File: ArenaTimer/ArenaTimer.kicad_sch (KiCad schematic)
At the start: 2 parts, among them U1 LM2596S-5

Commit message: finish up routing
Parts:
- removed A1: Adafruit_Feather_HUZZAH32_ESP32, Module:Adafruit_Feather, symbol MCU_Module:Adafruit_Feather_HUZZAH32_ESP32
- removed U1: LM2596S-5, Package_TO_SOT_SMD:TO-263-5_TabPin3, symbol Regulator_Switching:LM2596S-5
- added J1: POWER IN, TerminalBlock:TerminalBlock_Altech_AK300-2_P5.00mm, symbol Connector:Screw_Terminal_01x02
- added J2, J3: Conn_01x02_Pin, Connector_PinHeader_2.54mm:PinHeader_1x02_P2.54mm_Vertical, symbol Connector:Conn_01x02_Pin
- added J4, J6: GND, Connector_PinHeader_2.54mm:PinHeader_1x04_P2.54mm_Vertical, symbol Connector:Conn_01x04_Pin
- added J5, J7: 5V, Connector_PinHeader_2.54mm:PinHeader_1x04_P2.54mm_Vertical, symbol Connector:Conn_01x04_Pin
- added JP1: Jumper_2_Open, Jumper:SolderJumper-2_P1.3mm_Open_RoundedPad1.0x1.5mm, symbol Jumper:Jumper_2_Open
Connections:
- net TimerBorder/DIN: now also J2.2 (Pin_2), JP1.1 (A)
- net TimerBorder/DOUT: now also J3.2 (Pin_2)
- net TimerColon/DOUT: now also J3.1 (Pin_1), JP1.2 (B)
- new net +5V: J1.2 (Pin_2), J5.1 (Pin_1), J5.2 (Pin_2), J5.3 (Pin_3), J5.4 (Pin_4), J7.1 (Pin_1), J7.2 (Pin_2), J7.3 (Pin_3), J7.4 (Pin_4)
- new net GND: J1.1 (Pin_1), J4.1 (Pin_1), J4.2 (Pin_2), J4.3 (Pin_3), J4.4 (Pin_4), J6.1 (Pin_1), J6.2 (Pin_2), J6.3 (Pin_3), J6.4 (Pin_4)
- new net TimerDigit6/DIN: J2.1 (Pin_1)
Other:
- removed sheet TimerBorder1
- removed sheet TimerColon1
- removed sheet TimerDigit1
- removed sheet TimerDigit2
- removed sheet TimerDigit3
- removed sheet TimerDigit4
- removed sheet TimerDigit5
- added sheet TimerDigit6 (TimerDigit.kicad_sch)
- note added: "2nd copy of board is rotated 180 and makes up the other half of the display"
- note added: "5V Power Input"
- note added: "IO IN"
- note added: "IO OUT"
- note added: "Power connections between boards"
- note removed: "Back Side"
- note removed: "Front Side"
- note removed: "MCU ...."
- note removed: "Power 5V, 3A"

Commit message: add 3d models
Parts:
- removed J1: POWER IN, TerminalBlock:TerminalBlock_Altech_AK300-2_P5.00mm, symbol Connector:Screw_Terminal_01x02
- removed J2: Conn_01x02_Pin, Connector_PinHeader_2.54mm:PinHeader_1x02_P2.54mm_Vertical, symbol Connector:Conn_01x02_Pin
- removed J6: GND, Connector_PinHeader_2.54mm:PinHeader_1x04_P2.54mm_Vertical, symbol Connector:Conn_01x04_Pin
- removed J7: 5V, Connector_PinHeader_2.54mm:PinHeader_1x04_P2.54mm_Vertical, symbol Connector:Conn_01x04_Pin
- added D40: 1N1007, SMA, Diode_SMD:D_SMA, symbol Device:D
- added H1, H2, H3, H4, H5, H6, H7, H8, H9: MountingHole, MountingHole:MountingHole_3.2mm_M3, symbol Mechanical:MountingHole
- added J1: Blue ready-up, Connector_JST:JST_EH_S2B-EH_1x02_P2.50mm_Horizontal, symbol Connector:Conn_01x02_Socket
- added J10: Red ready-up, Connector_JST:JST_EH_S2B-EH_1x02_P2.50mm_Horizontal, symbol Connector:Conn_01x02_Socket
- added J11: Bell Power, TerminalBlock:TerminalBlock_bornier-2_P5.08mm, symbol Connector:Screw_Terminal_01x02
- added J12, J13: Screw_Terminal_01x03, TerminalBlock:TerminalBlock_bornier-3_P5.08mm, symbol Connector:Screw_Terminal_01x03
- added J15, J16: Conn_01x15_Socket, Connector_PinSocket_2.54mm:PinSocket_1x15_P2.54mm_Vertical, symbol Connector:Conn_01x15_Socket
- added J2: Conn_01x02_Socket, Connector_PinSocket_2.54mm:PinSocket_1x02_P2.54mm_Horizontal, symbol Connector:Conn_01x02_Socket
- added J6: GND, Connector_PinSocket_2.54mm:PinSocket_1x04_P2.54mm_Horizontal, symbol Connector:Conn_01x04_Socket
- added J7: 5V, Connector_PinSocket_2.54mm:PinSocket_1x04_P2.54mm_Horizontal, symbol Connector:Conn_01x04_Socket
- added J8: Barrel_Jack, Connector_BarrelJack:BarrelJack_Horizontal, symbol Connector:Barrel_Jack
- added J9: Conn_01x06_Pin, Connector_JST:JST_EH_S6B-EH_1x06_P2.50mm_Horizontal, symbol Connector:Conn_01x06_Pin
- added K1: G5V-2_Split, Relay_THT:Relay_DPDT_Omron_G5V-2, symbol Relay:G5V-2_Split
- added Q1: BSS214NW, Package_TO_SOT_SMD:SOT-323_SC-70, symbol Transistor_FET:BSS214NW
- added R2: 100K, Resistor_SMD:R_0402_1005Metric, symbol Device:R_US
- J3: footprint Connector_PinHeader_2.54mm:PinHeader_1x02_P2.54mm_Vertical -> Connector_PinHeader_2.54mm:PinHeader_1x02_P2.54mm_Horizontal
- J4, J5: footprint Connector_PinHeader_2.54mm:PinHeader_1x04_P2.54mm_Vertical -> Connector_PinHeader_2.54mm:PinHeader_1x04_P2.54mm_Horizontal
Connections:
- net +5V: now also JP1.2 (B), D40.1 (K), J15.15 (Pin_15), J7.1 (Pin_1), J7.2 (Pin_2), J7.3 (Pin_3), J7.4 (Pin_4), J8.1, K1.1
- net GND: now also J1.2 (Pin_2), J10.2 (Pin_2), J11.2 (Pin_2), J12.3 (Pin_3), J13.3 (Pin_3), J15.14 (Pin_14), J16.14 (Pin_14), J6.1 (Pin_1), J6.2 (Pin_2), J6.3 (Pin_3), J6.4 (Pin_4), J8.2, J9.6 (Pin_6), Q1.2 (S), R2.2
- net TimerColon/DOUT: no longer JP1.2 (B)
- net TimerBorder/DIN: no longer names the net of JP1.1 (A)
- net TimerBorder/DIN: now also J11.1 (Pin_1), K1.13, K1.4
- new net: J12.1 (Pin_1), K1.6
- new net: J12.2 (Pin_2), K1.8
- new net: J13.1 (Pin_1), K1.11
- new net: J13.2 (Pin_2), K1.9
- new net: D40.2 (A), K1.16, Q1.3 (D)
- new net +3.3V: J16.15 (Pin_15)
- new net BORDER_LEDS: J16.9 (Pin_9), J2.1 (Pin_1)
- new net DIGIT_LEDS: J16.8 (Pin_8), J2.2 (Pin_2)
- new net RELAY_EN: J16.13 (Pin_13), Q1.1 (G), R2.1
- new net nBLUE_RDY_BTN: J1.1 (Pin_1)
- new net nBUZZER_BTN: J16.12 (Pin_12), J9.5 (Pin_5)
- new net nLEFT_RDY_BTN: J16.11 (Pin_11)
- new net nPAUSE_BTN: J15.11 (Pin_11), J9.2 (Pin_2)
- new net nRED_RDY_BTN: J10.1 (Pin_1)
- new net nRESET_BTN: J15.12 (Pin_12), J9.3 (Pin_3)
- new net nRIGHT_RDY_BTN: J16.10 (Pin_10)
- new net nSTART_BTN: J15.10 (Pin_10), J9.1 (Pin_1)
- new net nTIME_SEL: J15.13 (Pin_13), J9.4 (Pin_4)
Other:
- note added: "Button Inputs"
- note added: "D23 D22 TX0 RX0 D21 D19 D18 D5 TX2 RX2 D4 D2 D15 GND 3.3V"
- note added: "EN VP VN D34 D35 D32 D33 D25 D26 D27 D14 D12 D13 GND VIN"
- note added: "ESP32 Module"
- note added: "LED Display"
- note added: "Power Input"
- moved on the sheet: J3, J4, J5

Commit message: updated border animation
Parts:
- J1, J10, J11, J15, J16, J2, J3, J4, J5, J6, J7, J8, J9, K1: now not fitted; now left out of the parts list
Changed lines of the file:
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@@
 		(unit 1)
 		(exclude_from_sim no)
-		(in_bom yes)
+		(in_bom no)
 		(on_board yes)
-		(dnp no)
+		(dnp yes)
 		(property "Reference" "J1"
 			(at 160.782 177.292 0)
@@
 		(unit 2)
 		(exclude_from_sim no)
-		(in_bom yes)
+		(in_bom no)
 		(on_board yes)
-		(dnp no)
+		(dnp yes)
 		(fields_autoplaced yes)
 		(property "Reference" "K1"
@@
 		(unit 1)
 		(exclude_from_sim no)
-		(in_bom yes)
+		(in_bom no)
 		(on_board yes)
-		(dnp no)
+		(dnp yes)
 		(property "Reference" "J11"
 			(at 382.524 160.02 0)
@@
 		(unit 1)
 		(exclude_from_sim no)
-		(in_bom yes)
+		(in_bom no)
 		(on_board yes)
-		(dnp no)
+		(dnp yes)
 		(fields_autoplaced yes)
 		(property "Reference" "J5"
@@
 		(unit 3)
 		(exclude_from_sim no)
-		(in_bom yes)
+		(in_bom no)
 		(on_board yes)
-		(dnp no)
+		(dnp yes)
 		(fields_autoplaced yes)
 		(property "Reference" "K1"
@@
 		(unit 1)
 		(exclude_from_sim no)
-		(in_bom yes)
+		(in_bom no)
 		(on_board yes)
-		(dnp no)
+		(dnp yes)
 		(property "Reference" "J16"
 			(at 316.738 51.562 0)
@@
 		(unit 1)
 		(exclude_from_sim no)
-		(in_bom yes)
+		(in_bom no)
 		(on_board yes)
-		(dnp no)
+		(dnp yes)
 		(property "Reference" "J3"
 			(at 182.372 72.898 0)
@@
 		(unit 1)
 		(exclude_from_sim no)
-		(in_bom yes)
+		(in_bom no)
 		(on_board yes)
-		(dnp no)
+		(dnp yes)
 		(property "Reference" "J15"
 			(at 288.544 51.816 0)
@@
 		(unit 1)
 		(exclude_from_sim no)
-		(in_bom yes)
+		(in_bom no)
 		(on_board yes)
-		(dnp no)
+		(dnp yes)
 		(property "Reference" "J10"
 			(at 160.782 159.512 0)
@@
 		(unit 1)
 		(exclude_from_sim no)
-		(in_bom yes)
+		(in_bom no)
 		(on_board yes)
-		(dnp no)
+		(dnp yes)
 		(property "Reference" "J7"
 			(at 71.628 228.854 0)
@@
 		(unit 1)
 		(exclude_from_sim no)
-		(in_bom yes)
+		(in_bom no)
 		(on_board yes)
-		(dnp no)
+		(dnp yes)
 		(fields_autoplaced yes)
 		(property "Reference" "J8"
@@
 		(unit 1)
 		(exclude_from_sim no)
-		(in_bom yes)
+		(in_bom no)
 		(on_board yes)
-		(dnp no)
+		(dnp yes)
 		(property "Reference" "J4"
 			(at 51.562 199.898 0)
@@
 		(unit 1)
 		(exclude_from_sim no)
-		(in_bom yes)
+		(in_bom no)
 		(on_board yes)
-		(dnp no)
+		(dnp yes)
 		(property "Reference" "J6"
 			(at 71.628 199.644 0)
@@
 		(unit 1)
 		(exclude_from_sim no)
-		(in_bom yes)
+		(in_bom no)
 		(on_board yes)
-		(dnp no)
+		(dnp yes)
 		(fields_autoplaced yes)
 		(property "Reference" "K1"
@@
 		(unit 1)
 		(exclude_from_sim no)
-		(in_bom yes)
+		(in_bom no)
 		(on_board yes)
-		(dnp no)
+		(dnp yes)
 		(fields_autoplaced yes)
 		(property "Reference" "J9"
@@
 		(unit 1)
 		(exclude_from_sim no)
-		(in_bom yes)
+		(in_bom no)
 		(on_board yes)
-		(dnp no)
+		(dnp yes)
 		(fields_autoplaced yes)
 		(property "Reference" "J2"

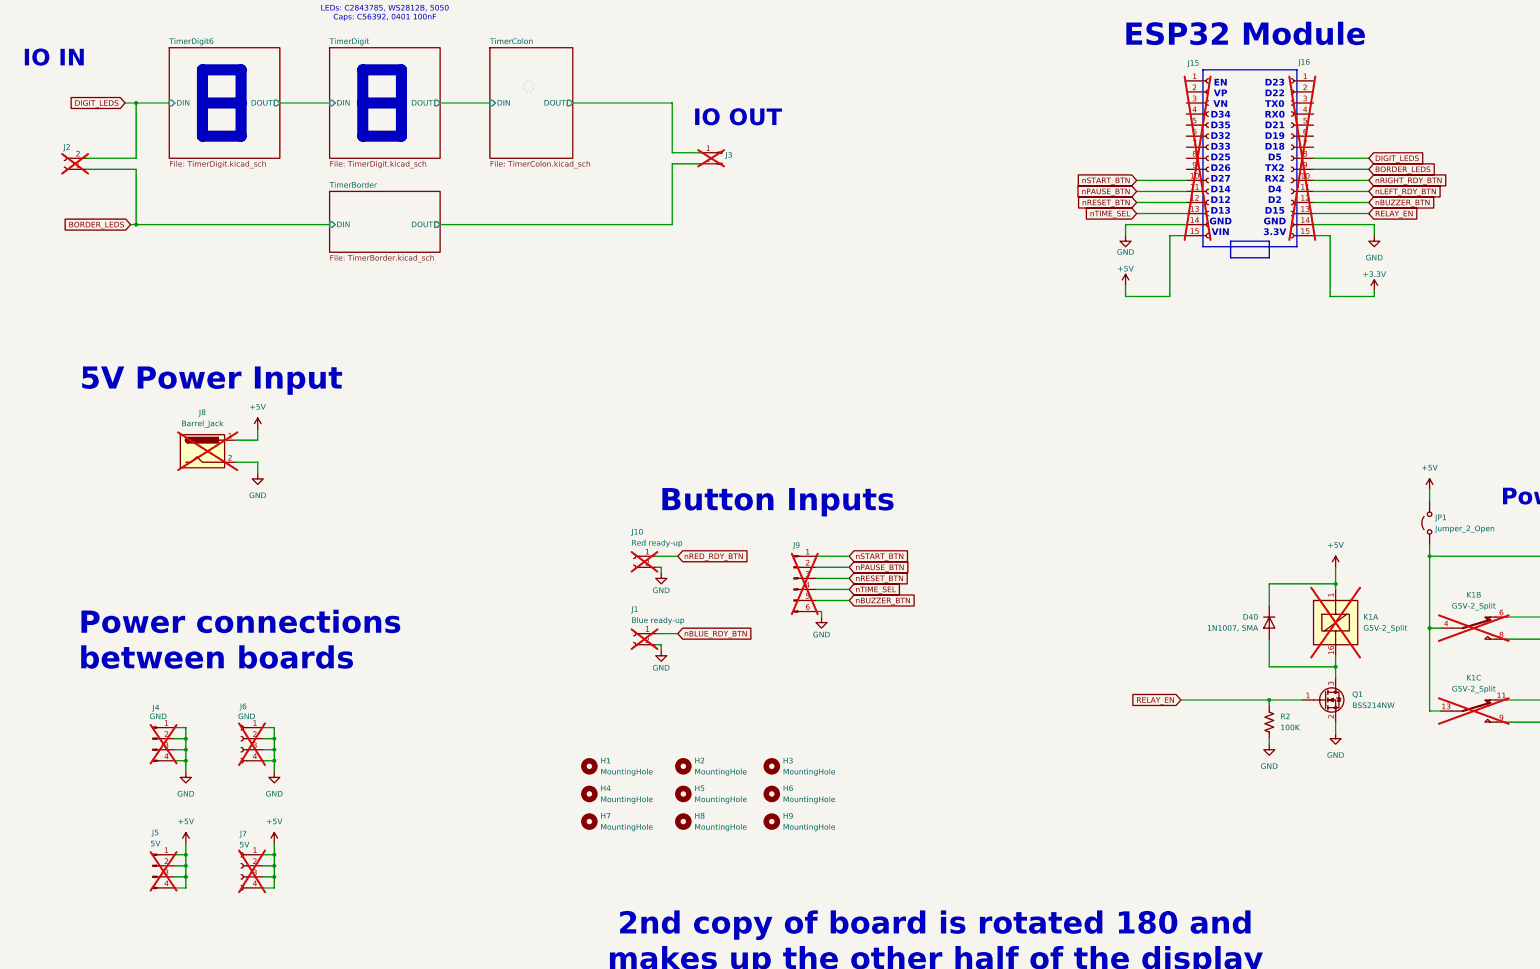
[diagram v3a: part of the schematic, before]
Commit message: PCB changes, code for TRC timers
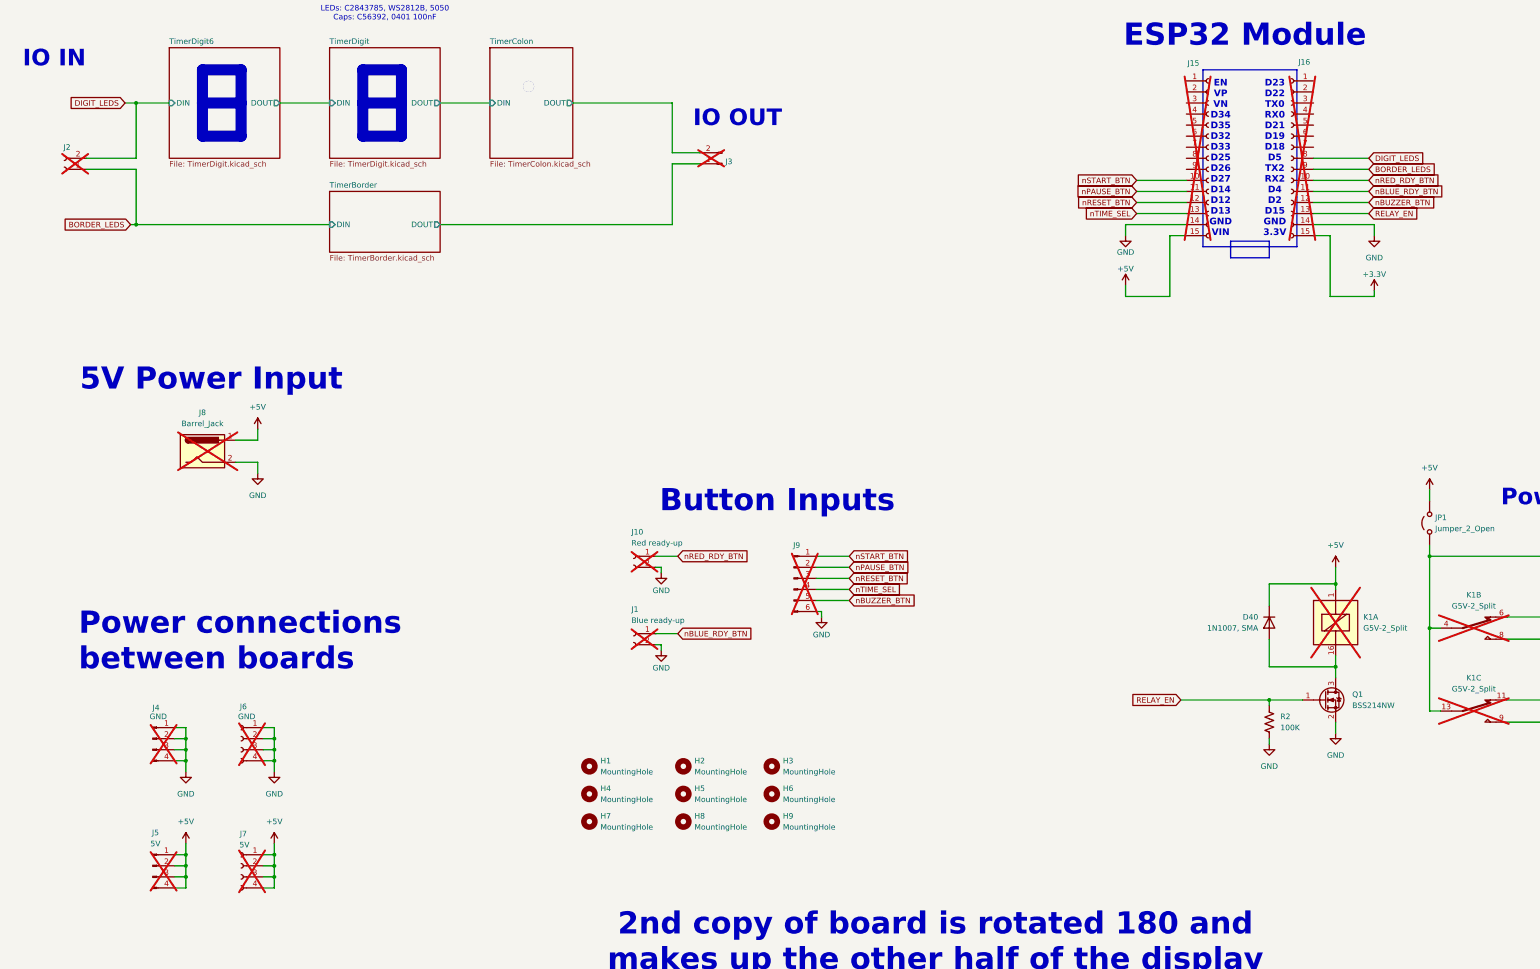
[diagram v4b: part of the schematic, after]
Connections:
- net nLEFT_RDY_BTN is gone; now on net nBLUE_RDY_BTN: J16.11 (Pin_11)
- net nRIGHT_RDY_BTN is gone; now on net nRED_RDY_BTN: J16.10 (Pin_10)
- net TimerBorder/DOUT: now also J3.1 (Pin_1); no longer J3.2 (Pin_2)
- net TimerColon/DOUT: now also J3.2 (Pin_2); no longer J3.1 (Pin_1)
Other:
- moved on the sheet: J3
